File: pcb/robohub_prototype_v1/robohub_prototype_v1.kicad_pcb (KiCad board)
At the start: 10 copper layers, 57 parts, among them J21 Barrel_Jack_Switch_Pin3Ring, J51 USB_A, J52 USB_A, U1 ATSAMA5D27C, U21 LM3880, U22 TPS564242DRL, U23 TPS564242DRL, U24 TPS564242DRL, U25 TPS564242DRL, U26 TPS564242DRL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

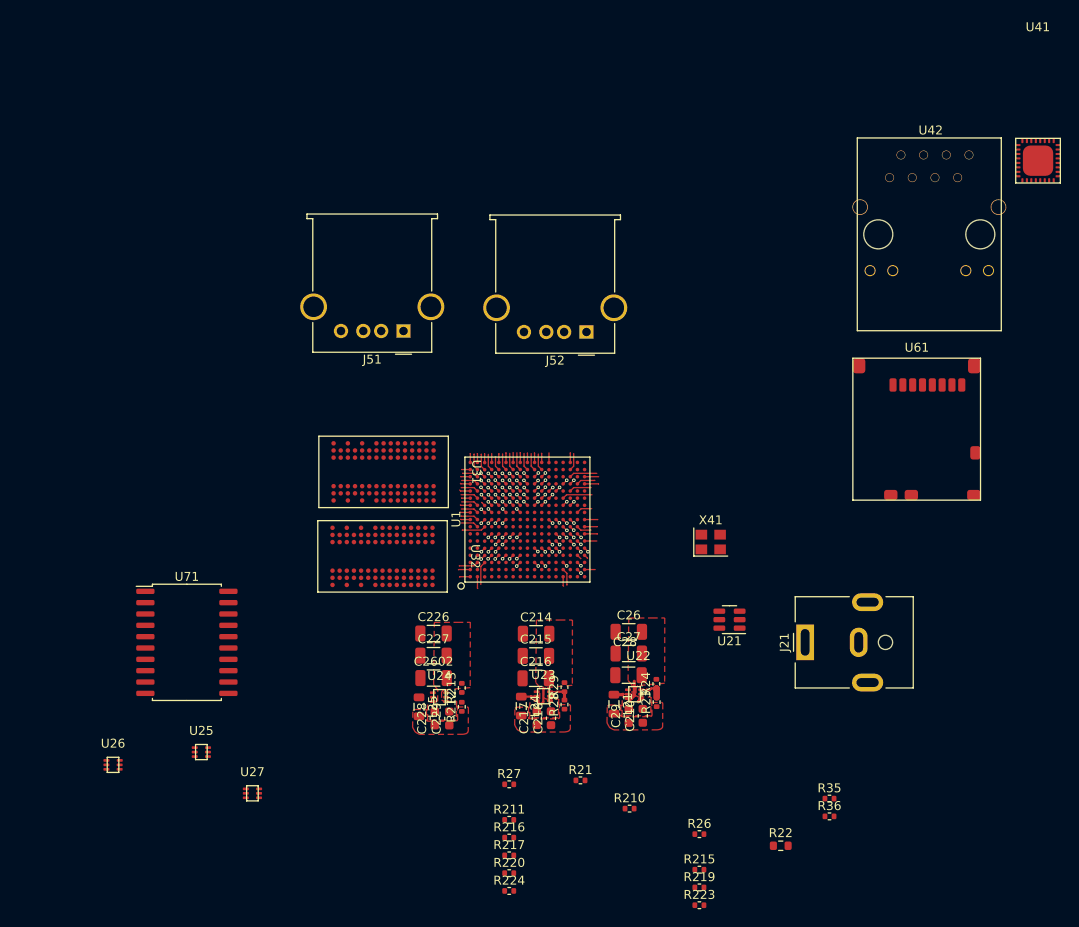
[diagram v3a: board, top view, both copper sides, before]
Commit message: Update paths for footprints top adjacent lib directory at above clone. Finish basic regulator layout/BOM. Link 3d STEPs into model. Rearrangle layout
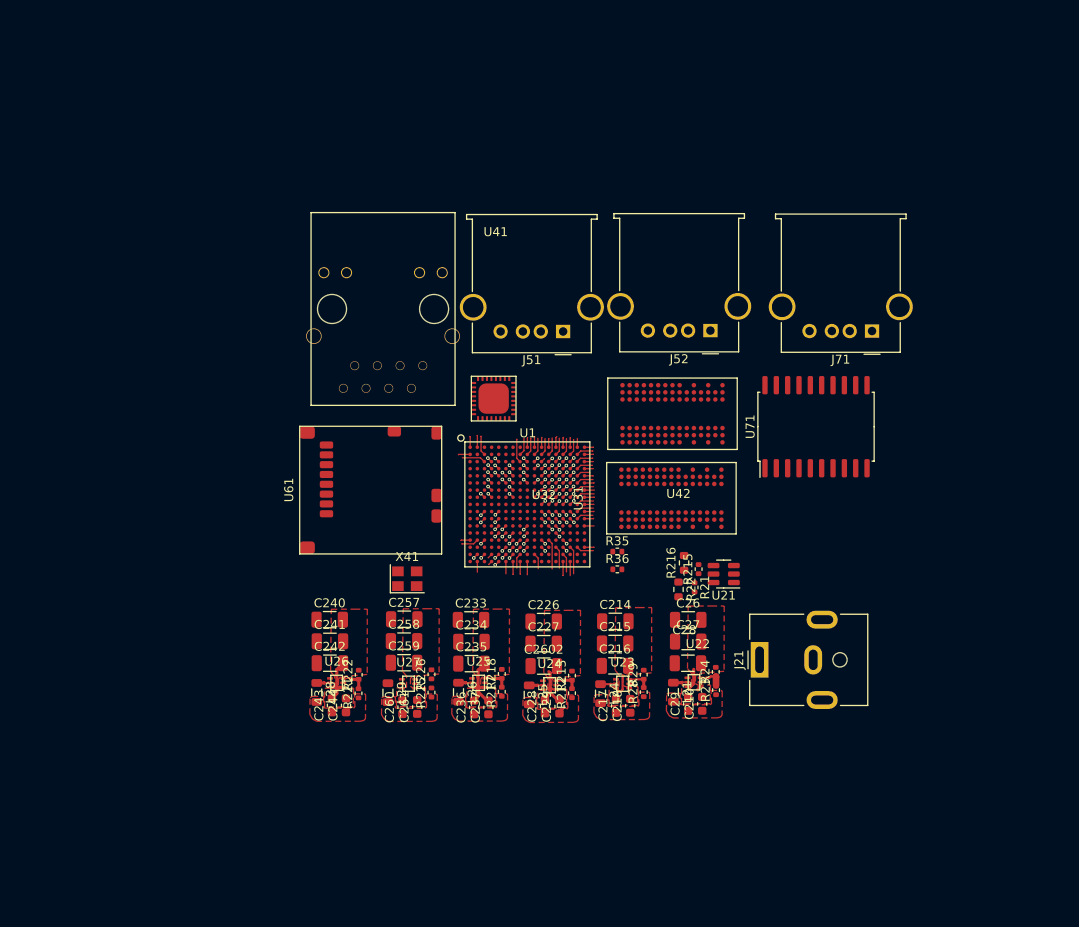
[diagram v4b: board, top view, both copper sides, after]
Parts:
- removed R210, R219, R223, R26: 100k, Resistor_SMD:R_0402_1005Metric
- removed R211, R220, R224, R27: 36.5k, Resistor_SMD:R_0402_1005Metric
- added C233: 10u, Capacitor_SMD:C_1206_3216Metric, F.Cu at (120.9, 105.4)
- added C234: 10u, Capacitor_SMD:C_1206_3216Metric, F.Cu at (121.0, 107.9)
- added C235: 0.1u, Capacitor_SMD:C_1206_3216Metric, F.Cu at (121.0, 110.3)
- added C236: 22u, Capacitor_SMD:C_0603_1608Metric, F.Cu at (121.3, 115.2)
- added C237: 22u, Capacitor_SMD:C_0603_1608Metric, F.Cu at (122.9, 115.2)
- added C240: 10u, Capacitor_SMD:C_1206_3216Metric, F.Cu at (105.1, 105.4)
- added C241: 10u, Capacitor_SMD:C_1206_3216Metric, F.Cu at (105.1, 107.8)
- added C242: 0.1u, Capacitor_SMD:C_1206_3216Metric, F.Cu at (105.1, 110.3)
- added C243: 22u, Capacitor_SMD:C_0603_1608Metric, F.Cu at (105.3, 115.0)
- added C244: 22u, Capacitor_SMD:C_0603_1608Metric, F.Cu at (106.9, 115.0)
- added C257: 10u, Capacitor_SMD:C_1206_3216Metric, F.Cu at (113.4, 105.4)
- added C258: 10u, Capacitor_SMD:C_1206_3216Metric, F.Cu at (113.4, 107.8)
- added C259: 0.1u, Capacitor_SMD:C_1206_3216Metric, F.Cu at (113.4, 110.2)
- added C260: 22u, Capacitor_SMD:C_0603_1608Metric, F.Cu at (113.2, 115.2)
- added C261: 22u, Capacitor_SMD:C_0603_1608Metric, F.Cu at (114.9, 115.2)
- added J71: USB_A, Connector_USB:USB_A_Molex_67643_Horizontal, F.Cu at (165.8, 73.1)
- added L26: 1u, Inductor_SMD:L_0805_2012Metric, F.Cu at (119.5, 113.5)
- added L28: 1u, Inductor_SMD:L_0805_2012Metric, F.Cu at (103.6, 113.6)
- added L29: 1u, Inductor_SMD:L_0805_2012Metric, F.Cu at (111.6, 113.6)
- added R218: 10k, Resistor_SMD:R_0402_1005Metric, F.Cu at (124.4, 111.5)
- added R221: 10k, Resistor_SMD:R_0402_1005Metric, F.Cu at (108.3, 113.7)
- added R222: 10k, Resistor_SMD:R_0402_1005Metric, F.Cu at (108.3, 111.6)
- added R225: 32k, Resistor_SMD:R_0402_1005Metric, F.Cu at (116.5, 113.6)
- added R226: 10k, Resistor_SMD:R_0402_1005Metric, F.Cu at (116.5, 111.5)
- L21, L24, L25: value 0.82u -> 2.2u
- R216: footprint Resistor_SMD:R_0402_1005Metric -> Resistor_SMD:R_0603_1608Metric
- moved U71 74.5 mm to (159.6, 83.8), turned to 90 degrees
- moved U41 66.5 mm to (123.5, 80.7)
- moved U42 61.7 mm to (111.1, 70.6), turned to 180 degrees
- moved U61 61.5 mm to (109.7, 90.9), turned to 90 degrees
- moved R216 36.5 mm to (144.8, 99.0), turned to 90 degrees
- moved R35 36.5 mm to (137.3, 97.8)
- moved R36 36.5 mm to (137.3, 99.8)
- moved U32 36.2 mm to (143.5, 82.3), turned to 90 degrees
- moved X41 34.2 mm to (113.8, 100.8)
- moved R215 33.7 mm to (146.4, 99.8), turned to 90 degrees
- moved U31 32.4 mm to (143.4, 91.8), turned to 90 degrees
- moved U25 32.0 mm to (121.8, 112.5)
- moved R22 30.9 mm to (144.2, 102.0), turned to -90 degrees
- moved U26 26.7 mm to (105.9, 112.5)
- moved R21 25.1 mm to (145.9, 101.8), turned to -90 degrees
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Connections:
- net Net-(U25-FB) renamed /Power Managment_2/VCC_1_2_FB
- R21 pad 2: /Power Managment_2/VCC_3A_EN -> /Power Managment_2/PS_GRP1_EN_DIV
- R215 pad 2: Net-(D24-K) -> /Power Managment_2/PS_GRP2_EN_DIV
- R216 pad 1: Net-(D24-K) -> /Power Managment_2/PS_GRP2_EN_DIV
- R22 pad 1: /Power Managment_2/VCC_3A_EN -> /Power Managment_2/PS_GRP1_EN_DIV
- U22 pad 5: /Power Managment_2/VCC_3A_EN -> /Power Managment_2/PS_GRP1_EN_DIV
- U23 pad 5: /Power Managment_2/VCC_3_3B_EN -> /Power Managment_2/PS_GRP1_EN_DIV
- U24 pad 5: /Power Managment_2/VCC_3_3C_EN -> /Power Managment_2/PS_GRP1_EN_DIV
- U25 pad 2: Net-(U25-SW) -> /Power Managment_2/VCC_1_2_SW
- U25 pad 5: Net-(D24-K) -> /Power Managment_2/PS_GRP2_EN_DIV
- U26 pad 2: Net-(U26-SW) -> /Power Managment_2/VCC_1_2_DDR_SW
- U26 pad 5: Net-(D25-K) -> /Power Managment_2/PS_GRP1_EN_DIV
- U26 pad 6: Net-(U26-FB) -> /Power Managment_2/VCC_1_2_DDR_FB
- U27 pad 5: Net-(D26-K) -> /Power Managment_2/PS_GRP2_EN_DIV
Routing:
- net GND: track 24.0 -> 44.4 mm
- net /Power Managment_2/VCC_1_2_DDR_FB: track 0.00 -> 2.84 mm
- net /Power Managment_2/VCC_1_2_FB: track 0.00 -> 2.82 mm
- net /Power Managment_2/VCC_3_3_C_FB: track 0.00 -> 2.71 mm
- net /Power Managment_2/VCC_3_3_C_SW: track 0.00 -> 1.56 mm
- net /Power Managment_2/VCC_1_2_SW: track 0.00 -> 1.53 mm
- net /Power Managment_2/VCC_1_2_DDR_SW: track 0.00 -> 1.49 mm
- added copper zone on F.Cu, net VCC_1_2
- added copper zone on F.Cu, net VCC_1_2_DDR
- added copper zone on F.Cu, net VCC_2_5
- added copper zone on F.Cu, net VCC_3_3_C

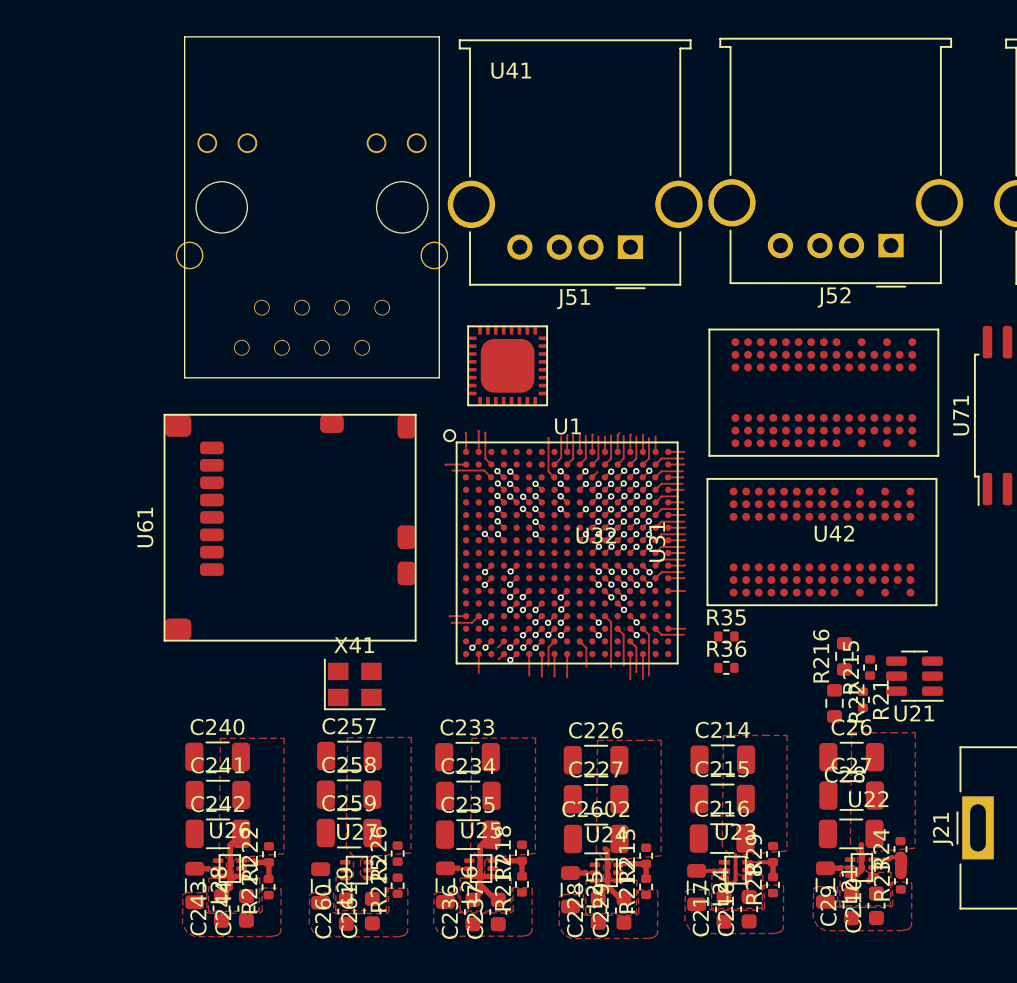
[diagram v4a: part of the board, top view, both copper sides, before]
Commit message: Add fuse to PCB design
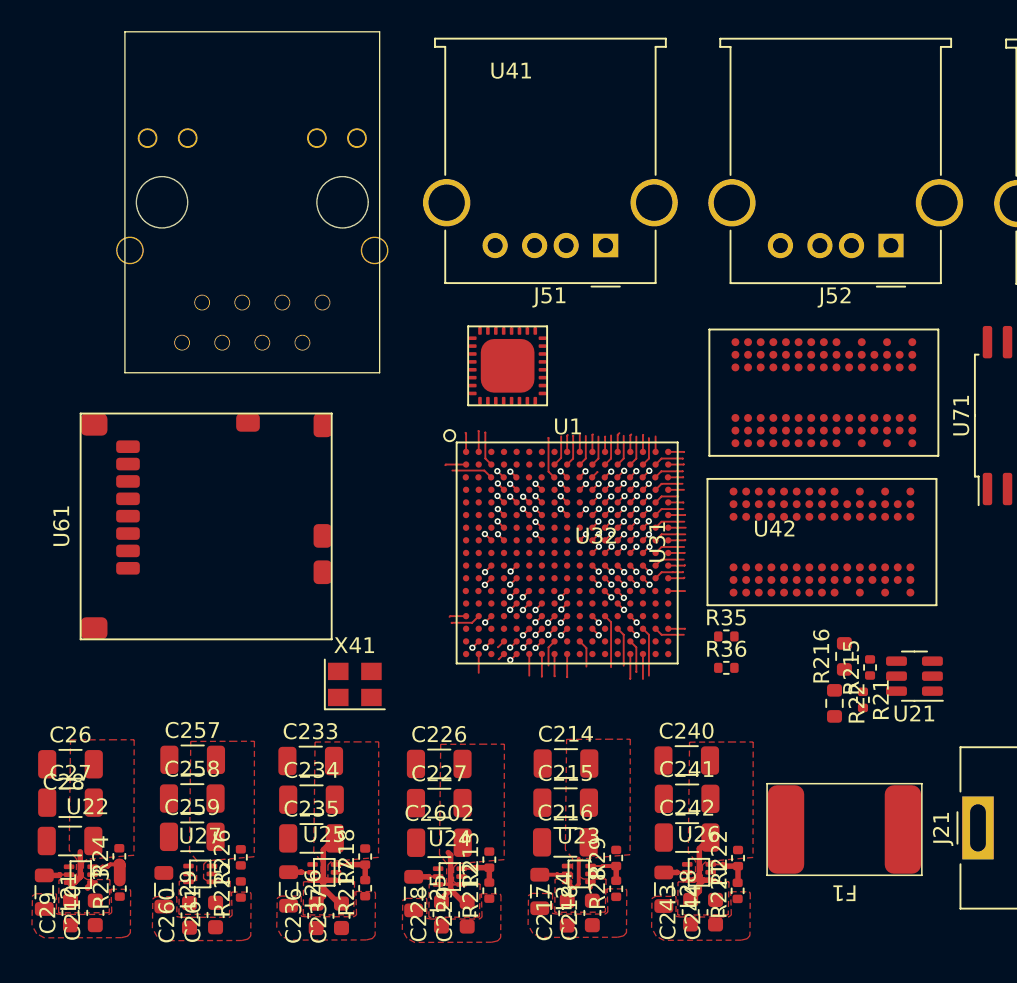
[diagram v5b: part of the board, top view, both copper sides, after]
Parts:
- added F1: Fuse, fryelabs_kicad_footprint_lib:0ZCF0050FF2C, F.Cu at (144.8, 110.0)
- moved C26 49.5 mm to (95.8, 105.9)
- moved C27 49.5 mm to (95.8, 108.3)
- moved C28 49.5 mm to (95.7, 110.7)
- moved C29 49.5 mm to (95.8, 115.3)
- moved C210 49.5 mm to (97.3, 115.3)
- moved L21 49.5 mm to (94.1, 114.0)
- moved R23 49.5 mm to (98.9, 113.8)
- moved R24 49.5 mm to (98.9, 111.7)
- moved U22 49.5 mm to (96.4, 112.9)
- moved C244 29.7 mm to (136.6, 115.2)
- moved C240 29.7 mm to (134.8, 105.6)
- moved C241 29.7 mm to (134.8, 108.1)
- moved C242 29.7 mm to (134.8, 110.5)
- moved C243 29.7 mm to (135.0, 115.2)
- moved L28 29.7 mm to (133.3, 113.8)
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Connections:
- J21 pad 1: 5V -> VCC

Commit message: Small updates to ACC signals for DDR2
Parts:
- R221: value 10k -> 20k
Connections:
- net VCC_1_2_DDR renamed VCC_1_8_DDR
- net VDDBU renamed VCC_3_3_A
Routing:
- removed copper zone on F.Cu, net VCC_1_8_DDR
